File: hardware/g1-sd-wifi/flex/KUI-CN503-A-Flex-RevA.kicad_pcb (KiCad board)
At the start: 2 copper layers, 10.7 x 59.9 mm, 2 parts, among them J1 CN503 row A solder contacts, J2 20-pin bottom-contact FPC tail

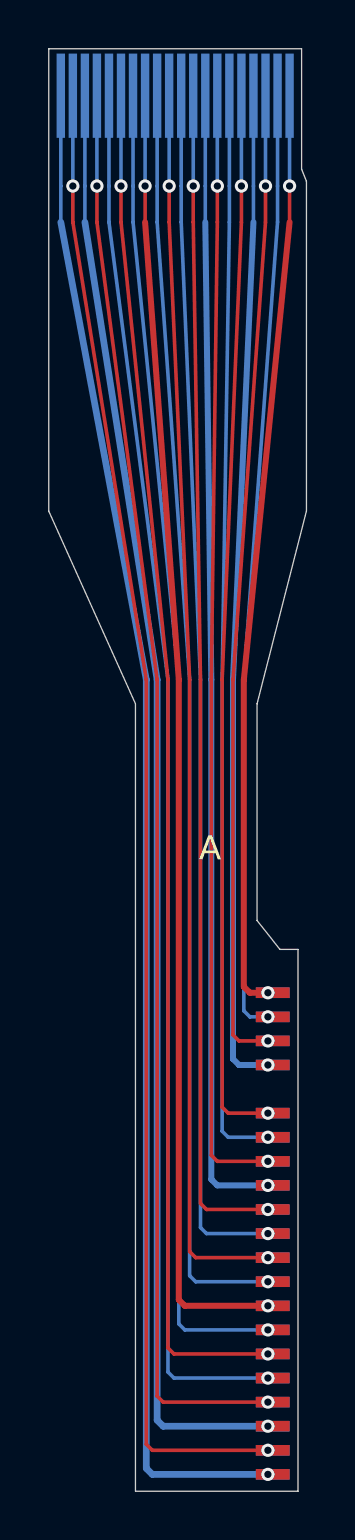
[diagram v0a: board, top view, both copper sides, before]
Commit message: G1 safety: fuse the host 3.3-V entry; no console 5 V on the flex or carrier
Host 3.3 V reached about 30 carrier parts straight from two flex contacts,
and the two console-5-V contacts were joined by an unused carrier trace;
a short on either would load a console supply through 0.5 A connector
contacts with no fuse anywhere. Now:

- F21 (0467.500NR, 0.5 A fast, same 467 family as F20) sits between the one
  remaining 3.3-V entry, J51 B1, and CONSOLE_3V3. If it opens the buffers
  lose VCCB and isolate, and U25 reports the host rail absent.
- CN503 A1 (second 3.3 V) and A3/B3 (5 V) get no flex copper at all: no
  landing pad, no trace, only an unconnected mating finger, so a chafed
  flex cannot short a console supply. Their carrier socket pins are bare.
  flex-interface.json lists them; the flex and carrier generators and both
  checks read that list. Flex ERC/DRC/parity 0; carrier ERC 0, integration
  check pass (362 parts).
- The DSN export keeps the 5-V and storage supply nets on the 1 oz outer
  layers: on 0.5 oz inner copper a 0.25 mm track at the fuse current would
  overheat (IPC-2221).
- F21 is placed by the floorplan next to J51; board DRC 0, parity 0
  (unrouted).

Co-Authored-By: Claude Opus 5.5 <noreply@anthropic.com>
Claude-Session: https://claude.ai/code/session_01Gp9EYc2r9fMpZ7V8WtfonZ
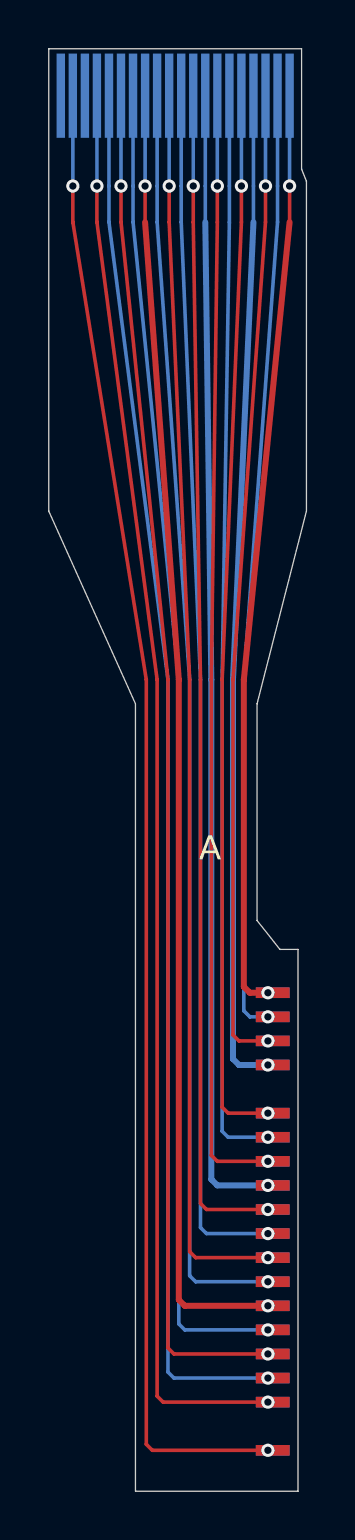
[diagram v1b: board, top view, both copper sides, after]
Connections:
- J2 pad 1: /CN503_A1_CONSOLE_3V3 -> unconnected-(J2-Pad1)
- J2 pad 3: /CN503_A3_CONSOLE_5V -> unconnected-(J2-Pad3)
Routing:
- net /CN503_A1_CONSOLE_3V3: track 62.9 -> 0.00 mm, vias 1 -> 0
- net /CN503_A3_CONSOLE_5V: track 60.3 -> 0.00 mm, vias 1 -> 0
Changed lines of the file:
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@@
 (setup (pad_to_mask_clearance 0) (allow_soldermask_bridges_in_footprints yes))
 (net 0 "")
-(net 1 "/CN503_A1_CONSOLE_3V3")
 (net 2 "/CN503_A2_ATA_RESETn")
-(net 3 "/CN503_A3_CONSOLE_5V")
 (net 4 "/CN503_A4_ATA_DD7")
 (net 5 "/CN503_A5_ATA_DD8")
@@
 (net 19 "/CN503_A20_ATA_CS0n")
 (net 20 "/CN503_A21_GND")
+(net 21 "unconnected-(J2-Pad1)")
+(net 22 "unconnected-(J2-Pad3)")
 (footprint "KUI_Flex:CN503_A_20_SolderLanding_1.00mm" (layer "F.Cu") (at 100.0 100.0) (attr board_only exclude_from_pos_files exclude_from_bom)
 (property "Reference" "J1" (at 0 0) (layer "F.Fab") (effects (font (size .8 .8)) hide))
 (property "Value" "CN503 row A solder contacts" (at 0 0) (layer "F.Fab") (effects (font (size .8 .8)) hide))
-(pad "1" smd rect (at -0.7 0) (size 1.4 .44) (layers "F.Cu" "F.Mask") (net 1 "/CN503_A1_CONSOLE_3V3") (solder_mask_margin .29))
-(pad "1" smd rect (at -0.7 0) (size 1.4 .44) (layers "B.Cu" "B.Mask") (net 1 "/CN503_A1_CONSOLE_3V3") (solder_mask_margin .29))
 (pad "2" smd rect (at -0.7 -1) (size 1.4 .44) (layers "F.Cu" "F.Mask") (net 2 "/CN503_A2_ATA_RESETn") (solder_mask_margin .29))
 (pad "2" smd rect (at -0.7 -1) (size 1.4 .44) (layers "B.Cu" "B.Mask") (net 2 "/CN503_A2_ATA_RESETn") (solder_mask_margin .29))
-(pad "3" smd rect (at -0.7 -2) (size 1.4 .44) (layers "F.Cu" "F.Mask") (net 3 "/CN503_A3_CONSOLE_5V") (solder_mask_margin .29))
-(pad "3" smd rect (at -0.7 -2) (size 1.4 .44) (layers "B.Cu" "B.Mask") (net 3 "/CN503_A3_CONSOLE_5V") (solder_mask_margin .29))
 (pad "4" smd rect (at -0.7 -3) (size 1.4 .44) (layers "F.Cu" "F.Mask") (net 4 "/CN503_A4_ATA_DD7") (solder_mask_margin .29))
 (pad "4" smd rect (at -0.7 -3) (size 1.4 .44) (layers "B.Cu" "B.Mask") (net 4 "/CN503_A4_ATA_DD7") (solder_mask_margin .29))
@@
 (property "Reference" "J2" (at 0 0) (layer "F.Fab") (effects (font (size .8 .8)) hide))
 (property "Value" "20-pin bottom-contact FPC tail" (at 0 0) (layer "F.Fab") (effects (font (size .8 .8)) hide))
-(pad "1" smd rect (at -9.5 -57.25) (size .35 3.5) (layers "B.Cu" "B.Mask") (net 1 "/CN503_A1_CONSOLE_3V3") (solder_mask_margin .10))
+(pad "1" smd rect (at -9.5 -57.25) (size .35 3.5) (layers "B.Cu" "B.Mask") (net 21 "unconnected-(J2-Pad1)") (solder_mask_margin .10))
 (pad "2" smd rect (at -9 -57.25) (size .35 3.5) (layers "B.Cu" "B.Mask") (net 2 "/CN503_A2_ATA_RESETn") (solder_mask_margin .10))
-(pad "3" smd rect (at -8.5 -57.25) (size .35 3.5) (layers "B.Cu" "B.Mask") (net 3 "/CN503_A3_CONSOLE_5V") (solder_mask_margin .10))
+(pad "3" smd rect (at -8.5 -57.25) (size .35 3.5) (layers "B.Cu" "B.Mask") (net 22 "unconnected-(J2-Pad3)") (solder_mask_margin .10))
 (pad "4" smd rect (at -8 -57.25) (size .35 3.5) (layers "B.Cu" "B.Mask") (net 4 "/CN503_A4_ATA_DD7") (solder_mask_margin .10))
 (pad "5" smd rect (at -7.5 -57.25) (size .35 3.5) (layers "B.Cu" "B.Mask") (net 5 "/CN503_A5_ATA_DD8") (solder_mask_margin .10))
@@
 (pad "20" smd rect (at -0 -57.25) (size .35 3.5) (layers "B.Cu" "B.Mask") (net 20 "/CN503_A21_GND") (solder_mask_margin .10))
 )
-(segment (start 99.3 100) (end 99.1 100) (width 0.15) (layer "F.Cu") (net 1))
-(segment (start 99.3 100) (end 99.1 100) (width 0.15) (layer "B.Cu") (net 1))
-(segment (start 99.1 100) (end 94.3 100) (width 0.28) (layer "B.Cu") (net 1))
-(segment (start 94.3 100) (end 94.05 99.75) (width 0.28) (layer "B.Cu") (net 1))
-(segment (start 94.05 99.75) (end 94.05 67) (width 0.28) (layer "B.Cu") (net 1))
-(segment (start 94.05 67) (end 90.5 48) (width 0.28) (layer "B.Cu") (net 1))
-(segment (start 90.5 48) (end 90.5 46.5) (width 0.15) (layer "B.Cu") (net 1))
-(segment (start 90.5 46.5) (end 90.5 42.75) (width 0.15) (layer "B.Cu") (net 1))
 (segment (start 99.3 99) (end 99.1 99) (width 0.15) (layer "F.Cu") (net 2))
 (segment (start 99.3 99) (end 99.1 99) (width 0.15) (layer "B.Cu") (net 2))
@@
 (segment (start 91 48) (end 91 46.5) (width 0.15) (layer "F.Cu") (net 2))
 (segment (start 91 46.5) (end 91 42.75) (width 0.15) (layer "B.Cu") (net 2))
-(segment (start 99.3 98) (end 99.1 98) (width 0.15) (layer "F.Cu") (net 3))
-(segment (start 99.3 98) (end 99.1 98) (width 0.15) (layer "B.Cu") (net 3))
-(segment (start 99.1 98) (end 94.75 98) (width 0.28) (layer "B.Cu") (net 3))
-(segment (start 94.75 98) (end 94.5 97.75) (width 0.28) (layer "B.Cu") (net 3))
-(segment (start 94.5 97.75) (end 94.5 67) (width 0.28) (layer "B.Cu") (net 3))
-(segment (start 94.5 67) (end 91.5 48) (width 0.28) (layer "B.Cu") (net 3))
-(segment (start 91.5 48) (end 91.5 46.5) (width 0.15) (layer "B.Cu") (net 3))
-(segment (start 91.5 46.5) (end 91.5 42.75) (width 0.15) (layer "B.Cu") (net 3))
 (segment (start 99.3 97) (end 99.1 97) (width 0.15) (layer "F.Cu") (net 4))
 (segment (start 99.3 97) (end 99.1 97) (width 0.15) (layer "B.Cu") (net 4))
@@
 (segment (start 100 48) (end 100 46.5) (width 0.15) (layer "F.Cu") (net 20))
 (segment (start 100 46.5) (end 100 42.75) (width 0.15) (layer "B.Cu") (net 20))
-(via (at 99.1 100) (size .55) (drill .3) (layers "F.Cu" "B.Cu") (net 1))
 (via (at 99.1 99) (size .55) (drill .3) (layers "F.Cu" "B.Cu") (net 2))
 (via (at 91 46.5) (size .55) (drill .3) (layers "F.Cu" "B.Cu") (net 2))
-(via (at 99.1 98) (size .55) (drill .3) (layers "F.Cu" "B.Cu") (net 3))
 (via (at 99.1 97) (size .55) (drill .3) (layers "F.Cu" "B.Cu") (net 4))
 (via (at 92 46.5) (size .55) (drill .3) (layers "F.Cu" "B.Cu") (net 4))
